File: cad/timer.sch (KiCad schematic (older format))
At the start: 16 parts, among them J1 Motor, J2 Pot, J4 Prog, Q2 S9013, Q3 S9012, U1 ATMEGA328P-PU, U2 LM393, U3 L293D, Y1 32.768kHz

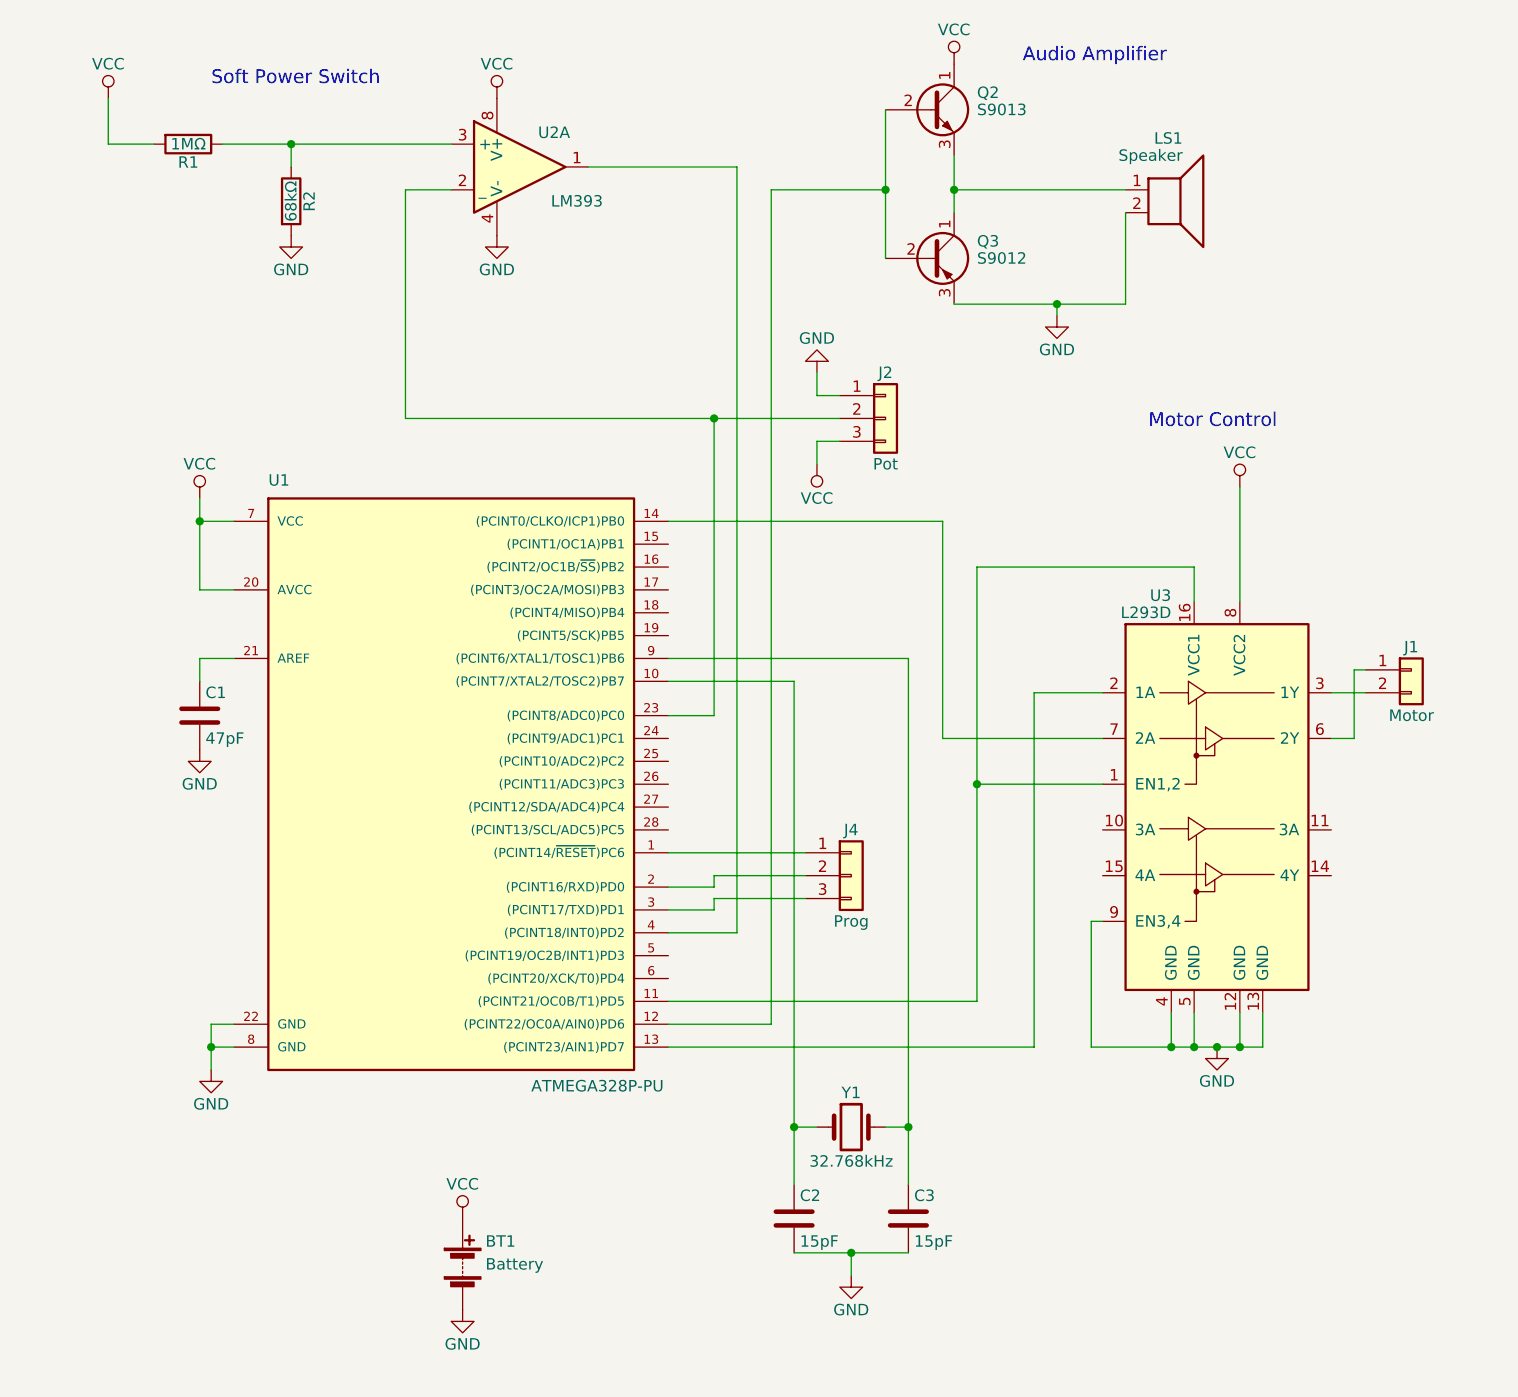
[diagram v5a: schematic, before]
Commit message: Schematic for updated design
- Now using MOSFETs for both motor and audio switching
- Added a bunch of bypass/decoupling capacitors
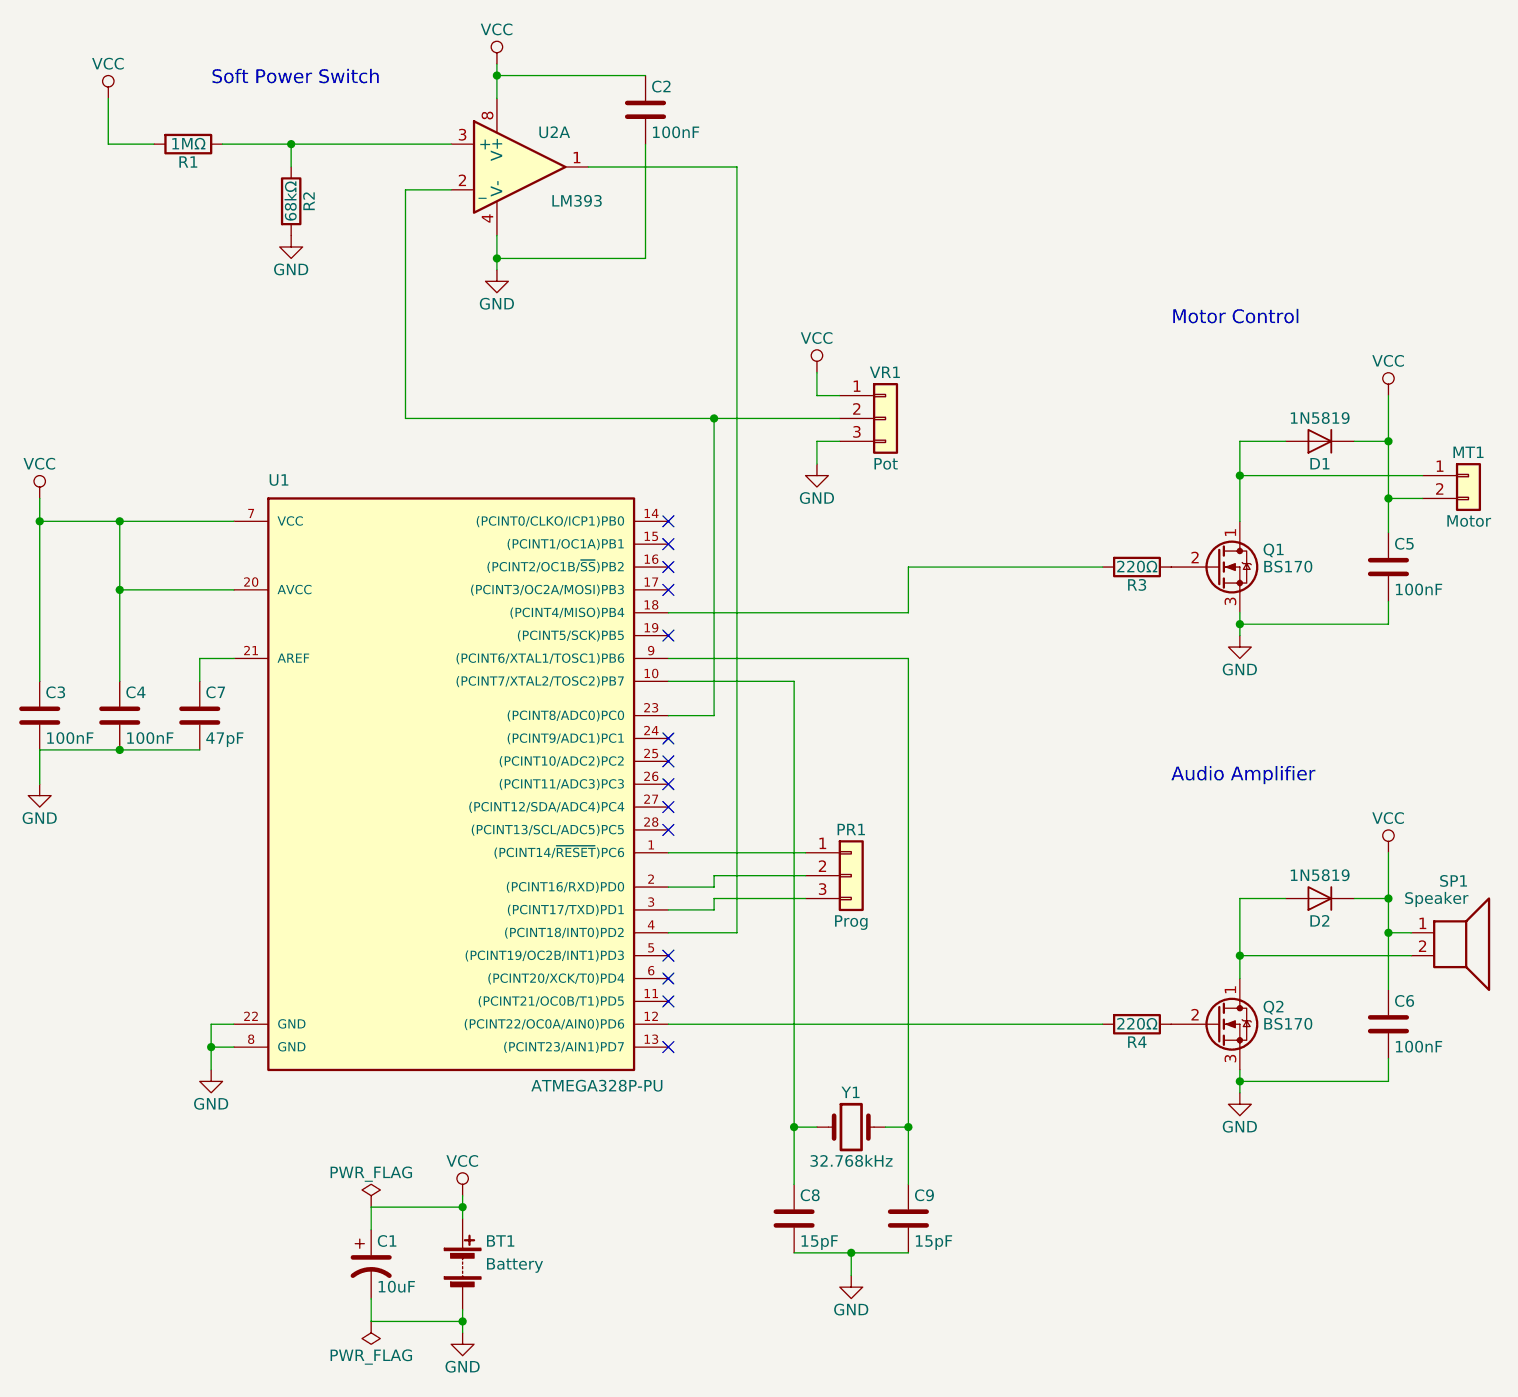
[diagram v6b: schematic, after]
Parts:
- removed Q2: S9013, TO_SOT_Packages_THT:TO-92_Inline_Wide, symbol BC337
- removed Q3: S9012, TO_SOT_Packages_THT:TO-92_Inline_Wide, symbol BC327
- removed U3: L293D, Housings_DIP:DIP-16_W7.62mm, symbol L293D
- added C1: 10uF, Capacitors_THT:CP_Radial_D5.0mm_P2.50mm, symbol CP1
- added C2, C3, C4, C5, C6: 100nF, Capacitors_THT:C_Disc_D5.0mm_W2.5mm_P5.00mm, symbol C
- added D1, D2: 1N5819, Diodes_THT:D_DO-41_SOD81_P2.54mm_Vertical_KathodeUp, symbol D
- added Q1, Q2: BS170, TO_SOT_Packages_THT:TO-92_Inline_Wide, symbol BS170
- added R3, R4: 220Ω, Resistors_THT:R_Axial_DIN0207_L6.3mm_D2.5mm_P2.54mm_Vertical, symbol R
- R1, R2: footprint Resistors_THT:R_Axial_DIN0207_L6.3mm_D2.5mm_P10.16mm_Horizontal -> Resistors_THT:R_Axial_DIN0207_L6.3mm_D2.5mm_P2.54mm_Vertical
- renumbered C1 to C7, C2 to C8, C3 to C9, J1 to MT1, J4 to PR1, LS1 to SP1, J2 to VR1
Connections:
- net GND: now also VR1.3 (Pin_3), C1.2, C2.2, C3.2, C4.2, C5.2, C6.2, Q1.3 (S), Q2.3 (S); no longer SP1.2, VR1.1 (Pin_1)
- net VCC: now also MT1.2 (Pin_2), SP1.1, VR1.1 (Pin_1), C1.1, C2.1, C3.1, C4.1, C5.1, C6.1, D1.1 (K), D2.1 (K); no longer VR1.3 (Pin_3)
- net at MT1.1 (Pin_1): now also D1.2 (A), Q1.1 (D)
- net at U1.12 ((PCINT22/OC0A/AIN0)PD6): now also R4.2
- net at U1.18 ((PCINT4/MISO)PB4): now also R3.2
- new net: D2.2 (A), Q2.1 (D), SP1.2
- new net: Q2.2 (G), R4.1
- new net: Q1.2 (G), R3.1
- no-connect marks 0 -> 14
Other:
- moved on the sheet: MT1, SP1

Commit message: Changes from new kicad version
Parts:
- BT1: symbol Battery -> Device:Battery
- C1: symbol CP1 -> Device:CP1
- C2, C3, C4, C5, C6, C7, C8, C9: symbol C -> Device:C
- D1, D2: symbol D -> Device:D
- MT1: symbol Conn_01x02 -> timer-rescue:Conn_01x02
- PR1, VR1: symbol Conn_01x03 -> timer-rescue:Conn_01x03
- Q1, Q2: symbol BS170 -> timer-rescue:BS170
- R1, R2, R3, R4: symbol R -> Device:R
- SP1: symbol Speaker -> Device:Speaker
- U1: symbol ATMEGA328P-PU -> timer-rescue:ATMEGA328P-PU
- U2: symbol LM393 -> timer-rescue:LM393
- Y1: symbol Crystal -> Device:Crystal
